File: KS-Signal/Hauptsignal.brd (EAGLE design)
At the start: 24.6 x 48 mm, 10 parts

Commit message: ZwischenS1
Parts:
- added IC1: ATTINY44SSU, Attiny:SO14
- added R1, R2, R3, R4, R5, R6, R7, R8, R9: (no value), rcl:R0603
- turned LED10 to 270 degrees
- turned LED7 to 270 degrees
- turned LED8 to 270 degrees
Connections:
- net N$1 renamed GN
- new net GE: LED9.+
- new net N$1: LED9.-, R9.1
- new net N$2: LED6.-, R6.1
- new net N$3: LED8.-, R5.1
- new net N$4: LED5.-, R4.1
- new net N$5: LED10.-, R3.1
- new net N$6: LED7.-, R2.1
- new net N$7: LED1.-, R1.1
- new net N$8: LED3.-, LED4.-, R7.1
- new net N$9: LED2.-, R8.1
- new net RT: LED2.+
- new net SH1: LED7.+
- new net SH1ZS1: LED1.+
- new net VCC: IC1.1
- new net ZL: LED6.+
- new net ZS7: LED10.+, LED5.+, LED8.+
- net GND: now also IC1.14, R1.2, R2.2, R3.2, R4.2, R5.2, R6.2, R7.2, R8.2, R9.2; no longer LED1.-, LED10.-, LED2.-, LED3.-, LED4.-, LED5.-, LED6.-, LED7.-, LED8.-, LED9.-
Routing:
- net GN: track 0.80 -> 0.00 mm
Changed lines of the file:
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@@
 <?xml version="1.0" encoding="utf-8"?>
 <!DOCTYPE eagle SYSTEM "eagle.dtd">
-<eagle version="8.2.2">
+<eagle version="8.3.2">
 <drawing>
 <settings>
 <setting alwaysvectorfont="no"/>
+<setting keepoldvectorfont="yes"/>
 <setting verticaltext="up"/>
 </settings>
@@
 <elements>
 <element name="LED1" library="LEDFLATTOP" package="3MM_FLAT_SMDLED" value="LED_SMD3MM" x="12.3" y="16.5" rot="R90"/>
-<element name="LED10" library="LEDFLATTOP" package="3MM_FLAT_SMDLED" value="LED_SMD3MM" x="8.77" y="16.5" rot="R90"/>
+<element name="LED10" library="LEDFLATTOP" package="3MM_FLAT_SMDLED" value="LED_SMD3MM" x="8.77" y="16.5" rot="R270"/>
 <element name="LED2" library="LEDFLATTOP" package="5MM_FLAT_SMDLED" value="LED_SMD5MM" x="12.3" y="35.4" rot="R180"/>
 <element name="LED3" library="LEDFLATTOP" package="5MM_FLAT_SMDLED" value="LED_SMD5MM" x="6" y="25.5"/>
@@
 <element name="LED5" library="LEDFLATTOP" package="3MM_FLAT_SMDLED" value="LED_SMD3MM" x="12.3" y="9.5"/>
 <element name="LED6" library="LEDFLATTOP" package="3MM_FLAT_SMDLED" value="LED_SMD3MM" x="5.2" y="42.8" rot="R45"/>
-<element name="LED7" library="LEDFLATTOP" package="3MM_FLAT_SMDLED" value="LED_SMD3MM" x="3.86" y="9.5" rot="R90"/>
-<element name="LED8" library="LEDFLATTOP" package="3MM_FLAT_SMDLED" value="LED_SMD3MM" x="15.83" y="16.5" rot="R90"/>
+<element name="LED7" library="LEDFLATTOP" package="3MM_FLAT_SMDLED" value="LED_SMD3MM" x="3.86" y="9.5" rot="R270"/>
+<element name="LED8" library="LEDFLATTOP" package="3MM_FLAT_SMDLED" value="LED_SMD3MM" x="15.83" y="16.5" rot="R270"/>
 <element name="LED9" library="LEDFLATTOP" package="5MM_FLAT_SMDLED" value="LED_SMD5MM" x="18.6" y="25.5"/>
+<element name="R1" library="rcl" package="R0603" value="" x="5.4" y="20.4"/>
+<element name="R2" library="rcl" package="R0603" value="" x="7.8" y="6.3" rot="R90"/>
+<element name="R3" library="rcl" package="R0603" value="" x="18.6" y="6.3" rot="R90"/>
+<element name="R4" library="rcl" package="R0603" value="" x="16.5" y="6.3" rot="R90"/>
+<element name="R5" library="rcl" package="R0603" value="" x="20.7" y="6.3" rot="R90"/>
+<element name="R6" library="rcl" package="R0603" value="" x="11.7" y="44.1" rot="R180"/>
+<element name="R7" library="rcl" package="R0603" value="" x="19.8" y="18.6" rot="R90"/>
+<element name="R8" library="rcl" package="R0603" value="" x="5.4" y="35.4"/>
+<element name="R9" library="rcl" package="R0603" value="" x="22.2" y="18.6" rot="R90"/>
+<element name="IC1" library="Attiny" package="SO14" value="ATTINY44SSU" x="12.3" y="30.3" rot="MR0"/>
 </elements>
 <signals>
@@
 <polygon width="0.1524" layer="1">
 <vertex x="-0.9" y="49.2"/>
-<vertex x="25.5" y="49.2"/>
-<vertex x="25.5" y="-0.9"/>
+<vertex x="25.8" y="49.5"/>
+<vertex x="25.8" y="-0.6"/>
 <vertex x="-0.9" y="-0.9"/>
 </polygon>
+<contactref element="IC1" pad="14"/>
+<contactref element="R1" pad="2"/>
+<contactref element="R2" pad="2"/>
+<contactref element="R3" pad="2"/>
+<contactref element="R4" pad="2"/>
+<contactref element="R5" pad="2"/>
+<contactref element="R6" pad="2"/>
+<contactref element="R8" pad="2"/>
+<contactref element="R7" pad="2"/>
+<contactref element="R9" pad="2"/>
+<wire x1="6.25" y1="35.4" x2="16.11" y2="33.3734" width="0" layer="19" extent="1-16"/>
+</signal>
+<signal name="GE">
+<contactref element="LED9" pad="+"/>
+</signal>
+<signal name="GN">
+<contactref element="LED4" pad="+"/>
+<contactref element="LED3" pad="+"/>
+<wire x1="8.75" y1="25.5" x2="9.55" y2="25.5" width="0" layer="19" extent="1-1"/>
+</signal>
+<signal name="RT">
+<contactref element="LED2" pad="+"/>
+</signal>
+<signal name="VCC">
+<contactref element="IC1" pad="1"/>
+</signal>
+<signal name="N$2">
+<contactref element="R6" pad="1"/>
+<contactref element="LED6" pad="-"/>
+<wire x1="3.9625625" y1="41.5625625" x2="12.55" y2="44.1" width="0" layer="19" extent="1-1"/>
+</signal>
+<signal name="N$3">
+<contactref element="R5" pad="1"/>
+<contactref element="LED8" pad="-"/>
+<wire x1="20.7" y1="5.45" x2="15.83" y2="18.25" width="0" layer="19" extent="1-1"/>
+</signal>
+<signal name="N$4">
+<contactref element="R4" pad="1"/>
+<contactref element="LED5" pad="-"/>
+<wire x1="10.55" y1="9.5" x2="16.5" y2="5.45" width="0" layer="19" extent="1-1"/>
+</signal>
+<signal name="N$5">
+<contactref element="LED10" pad="-"/>
+<contactref element="R3" pad="1"/>
+<wire x1="18.6" y1="5.45" x2="8.77" y2="18.25" width="0" layer="19" extent="1-1"/>
+</signal>
+<signal name="N$6">
+<contactref element="LED7" pad="-"/>
+<contactref element="R2" pad="1"/>
+<wire x1="7.8" y1="5.45" x2="3.86" y2="11.25" width="0" layer="19" extent="1-1"/>
+</signal>
+<signal name="N$7">
+<contactref element="R1" pad="1"/>
 <contactref element="LED1" pad="-"/>
-<contactref element="LED7" pad="-"/>
-<contactref element="LED10" pad="-"/>
-<contactref element="LED5" pad="-"/>
-<contactref element="LED8" pad="-"/>
-<contactref element="LED6" pad="-"/>
-<contactref element="LED2" pad="-"/>
+<wire x1="12.3" y1="14.75" x2="4.55" y2="20.4" width="0" layer="19" extent="1-1"/>
+</signal>
+<signal name="SH1ZS1">
+<contactref element="LED1" pad="+"/>
+</signal>
+<signal name="SH1">
+<contactref element="LED7" pad="+"/>
+</signal>
+<signal name="ZS7">
+<contactref element="LED10" pad="+"/>
+<contactref element="LED5" pad="+"/>
+<contactref element="LED8" pad="+"/>
+<wire x1="14.05" y1="9.5" x2="15.83" y2="14.75" width="0" layer="19" extent="1-1"/>
+<wire x1="8.77" y1="14.75" x2="15.83" y2="14.75" width="0" layer="19" extent="1-1"/>
+</signal>
+<signal name="ZL">
+<contactref element="LED6" pad="+"/>
+</signal>
+<signal name="N$8">
 <contactref element="LED3" pad="-"/>
 <contactref element="LED4" pad="-"/>
+<contactref element="R7" pad="1"/>
+<wire x1="19.8" y1="17.75" x2="15.05" y2="25.5" width="0" layer="19" extent="1-1"/>
+<wire x1="3.25" y1="25.5" x2="15.05" y2="25.5" width="0" layer="19" extent="1-1"/>
+</signal>
+<signal name="N$1">
 <contactref element="LED9" pad="-"/>
-</signal>
-<signal name="N$1">
-<contactref element="LED3" pad="+"/>
-<contactref element="LED4" pad="+"/>
-<wire x1="8.75" y1="25.5" x2="9.55" y2="25.5" width="0.1524" layer="1"/>
+<contactref element="R9" pad="1"/>
+<wire x1="22.2" y1="17.75" x2="15.85" y2="25.5" width="0" layer="19" extent="1-1"/>
+</signal>
+<signal name="N$9">
+<contactref element="R8" pad="1"/>
+<contactref element="LED2" pad="-"/>
+<wire x1="4.55" y1="35.4" x2="15.05" y2="35.4" width="0" layer="19" extent="1-1"/>
 </signal>
 </signals>

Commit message: Rückseite fertig
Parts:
- added Q1: IRLML5203, transistor-power:MICRO3
- added R10: (no value), rcl:R0603
- added X1: SSW-106-02-S-S-RA, con-samtec:SSW-106-02-S-S-RA
- added X2: TSW-106-02-S-S-RA, con-samtec:TSW-106-02-S-S-RA
- LED1, LED10, LED5, LED6, LED7, LED8: value LED_SMD3MM -> LED_SMD3MM_SMD/DIP; device LEDFLATTOP:3MM_FLAT_SMDLED -> LEDFLATTOP:3MM_FLAT/DIP_SMDLED
- LED2, LED3, LED4, LED9: value LED_SMD5MM -> LED_SMD5MM_SMD
- moved R3 18.2 mm to (6.00, 19.5), turned to 180 degrees
- moved R7 18.2 mm to (2.10, 22.8), turned to 270 degrees
- moved R8 13.2 mm to (18.6, 35.4)
- moved R5 12.8 mm to (18.6, 18.9), turned to 0 degrees
- moved R6 9.73 mm to (3.60, 38.7), turned to 270 degrees
- moved R2 9.26 mm to (3.90, 14.7)
- moved R4 8.76 mm to (9.60, 11.7)
- moved R9 7.38 mm to (15.6, 21.9), turned to 270 degrees
- moved R1 6.01 mm to (11.4, 20.7), turned to 180 degrees
- moved IC1 3.60 mm to (12.3, 26.7), turned to 90 degrees
- turned LED1 to 270 degrees
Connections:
- new net MISO: IC1.8, X1.2, X2.2
- new net N$10: LED10.+, LED5.+, LED8.+, Q1.3
- new net N$11: Q1.1, R10.2
- new net RESET: IC1.4, X1.5, X2.5
- new net SCL/SCK: IC1.9, X1.3, X2.3
- new net SDA/MOSI: IC1.7, X1.6, X2.6
- net GE: now also IC1.12
- net GN: now also IC1.11
- net GND: now also X1.1, X2.1
- net N$1: now also LED4.-
- net N$8: no longer LED4.-
- net RT: now also IC1.10
- net SH1: now also IC1.5
- net SH1ZS1: now also IC1.3
- net VCC: now also Q1.2, X1.4, X2.4
- net ZL: now also IC1.6
- net ZS7: now also IC1.2, R10.1; no longer LED10.+, LED5.+, LED8.+
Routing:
- net SH1: track 0.00 -> 25.3 mm
- net SH1ZS1: track 0.00 -> 22.7 mm
- net VCC: track 0.00 -> 21.4 mm
- net N$10: track 0.00 -> 18.8 mm
- net ZL: track 0.00 -> 18.3 mm
- net RT: track 0.00 -> 17.7 mm, vias 0 -> 1
- net GN: track 0.00 -> 16.3 mm, vias 0 -> 1
- net RESET: track 0.00 -> 16.0 mm
- net SCL/SCK: track 0.00 -> 12.1 mm
- net SDA/MOSI: track 0.00 -> 10.7 mm
- net MISO: track 0.00 -> 9.67 mm
- net GE: track 0.00 -> 9.19 mm, vias 0 -> 1
- net N$1: track 0.00 -> 2.85 mm
- net N$9: track 0.00 -> 2.70 mm
- net ZS7: track 0.00 -> 2.66 mm
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- added copper zone on layer 16, net GND

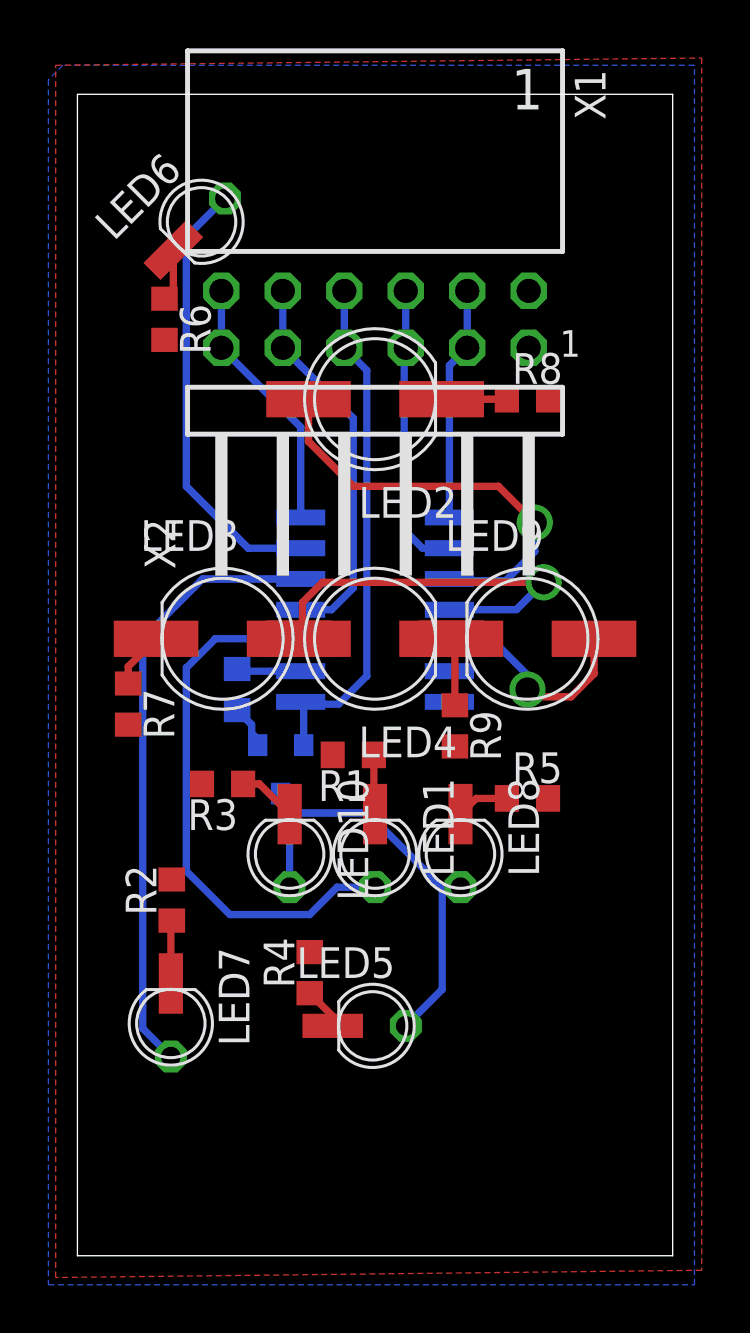
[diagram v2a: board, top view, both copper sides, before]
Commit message: Optimierung der Zusatzanzeiger & Hauptsignalplatine
- Symmetrischere Auslegung
- Entfernen von MISO/MISO connection zwischen Zusatzanzeiger und Hauptsignalschirm!
-> Zusatzanzeiger-MISO auf Signalschirmplatine nicht mehr connected (NC)
->mögliches Auslesen des DCC-Signals über den MISO-Anschluss (MOSI und SCK für I2C)
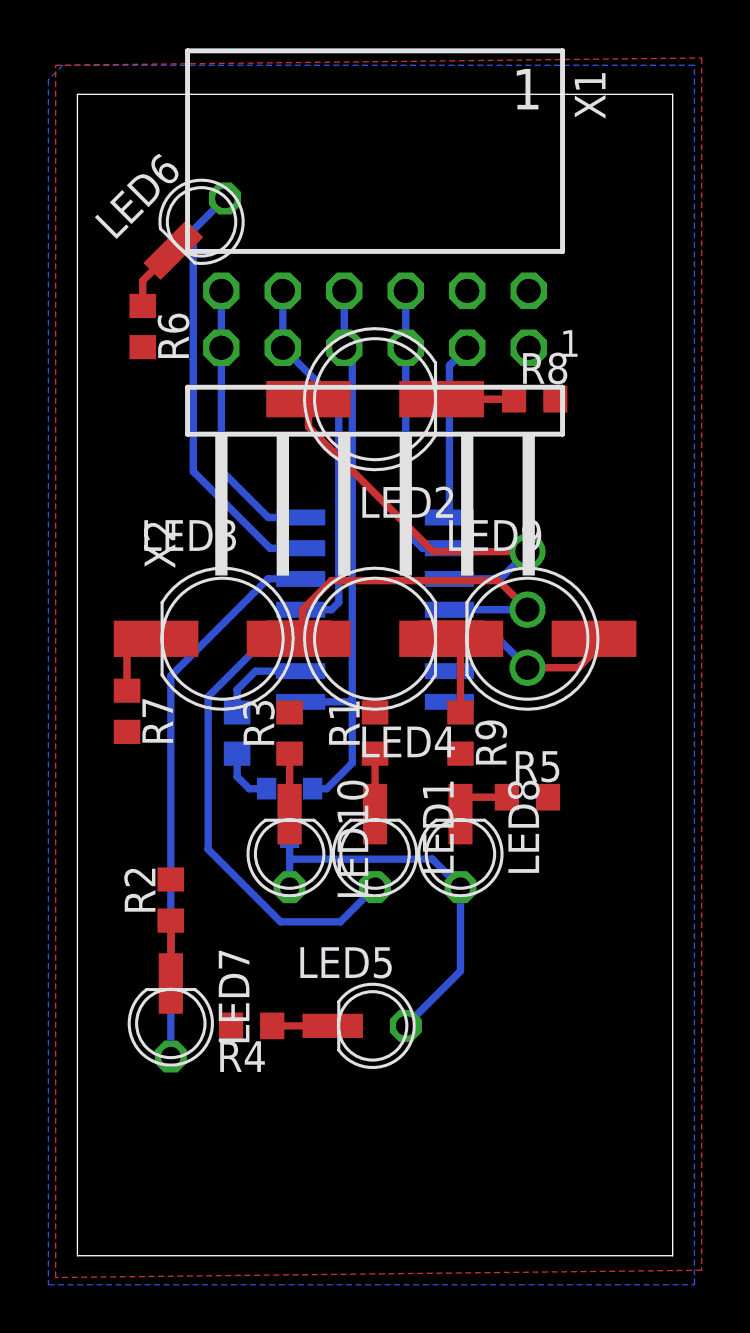
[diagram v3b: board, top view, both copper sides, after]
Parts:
- moved R3 3.48 mm to (8.77, 21.6), turned to 90 degrees
- moved R4 3.26 mm to (7.20, 9.50), turned to 180 degrees
- moved Q1 1.84 mm to (8.77, 18.3)
- moved R10 1.80 mm to (6.60, 21.6)
- moved R1 1.27 mm to (12.3, 21.6), turned to 90 degrees
- moved R6 0.95 mm to (2.70, 38.4)
- moved R9 0.38 mm to (15.8, 21.6)
- moved R7 0.30 mm to (2.05, 22.5)
- moved R8 0.30 mm to (18.9, 35.4)
- moved R5 0.05 mm to (18.6, 18.9)
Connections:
- new net NC: X1.2
- net MISO: no longer X1.2
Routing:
- net SH1ZS1: track 22.7 -> 19.9 mm
- net N$10: track 18.8 -> 16.3 mm
- net SH1: track 25.3 -> 22.8 mm
- net VCC: track 21.4 -> 23.9 mm
- net MISO: track 9.67 -> 7.32 mm
- net GE: track 9.19 -> 7.26 mm
- net RT: track 17.7 -> 16.1 mm
- net ZS7: track 2.66 -> 3.89 mm
- net N$8: track 2.33 -> 3.35 mm
- net N$1: track 2.85 -> 3.87 mm
- net SDA/MOSI: track 10.7 -> 11.5 mm
- net N$4: track 1.74 -> 2.50 mm
- net ZL: track 18.3 -> 17.6 mm
- net N$2: track 2.16 -> 2.84 mm
- net N$11: track 1.80 -> 2.38 mm
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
